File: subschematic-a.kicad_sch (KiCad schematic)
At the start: 0 parts

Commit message: chore(template): prepare Boardwright CI test
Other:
- title: Sheet Title A -> SUB SCHEMATIC A
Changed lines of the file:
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@@
 	(paper "A4")
 	(title_block
-		(title "Sheet Title A")
+		(title "SUB SCHEMATIC A")
 		(date "2025-01-12")
 		(rev "${REVISION}")
@@
 	(text_box "[${#}] ${TITLE}"
 		(exclude_from_sim no)
-		(at 99.06 15 0)
-		(size 107.9128 15)
+		(at 20.32 10.16 0)
+		(size 266.7 20.32)
 		(margins 4.4999 4.4999 4.4999 4.4999)
 		(stroke

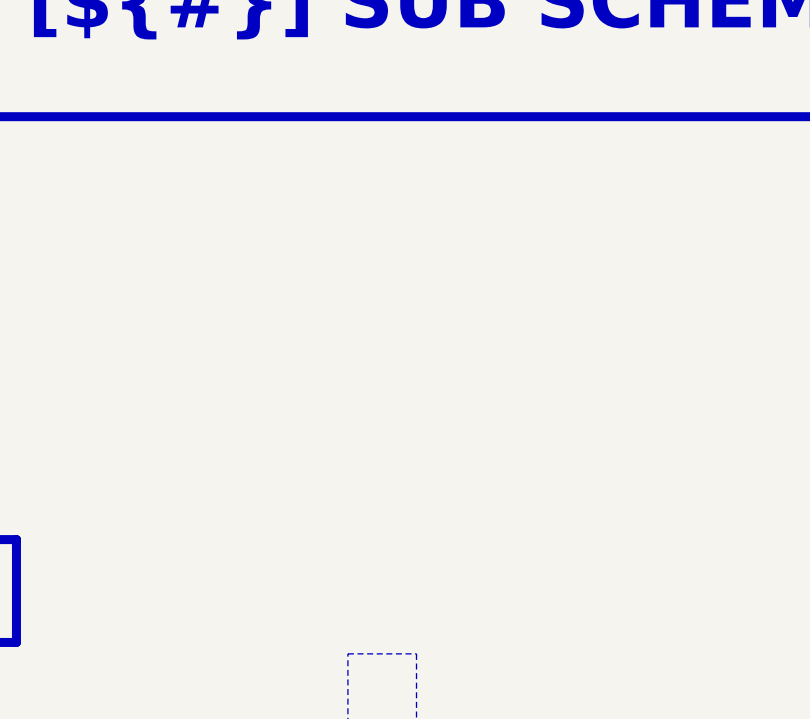
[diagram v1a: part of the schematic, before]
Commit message: feat(hardware): add Boardwright CI fixture circuit
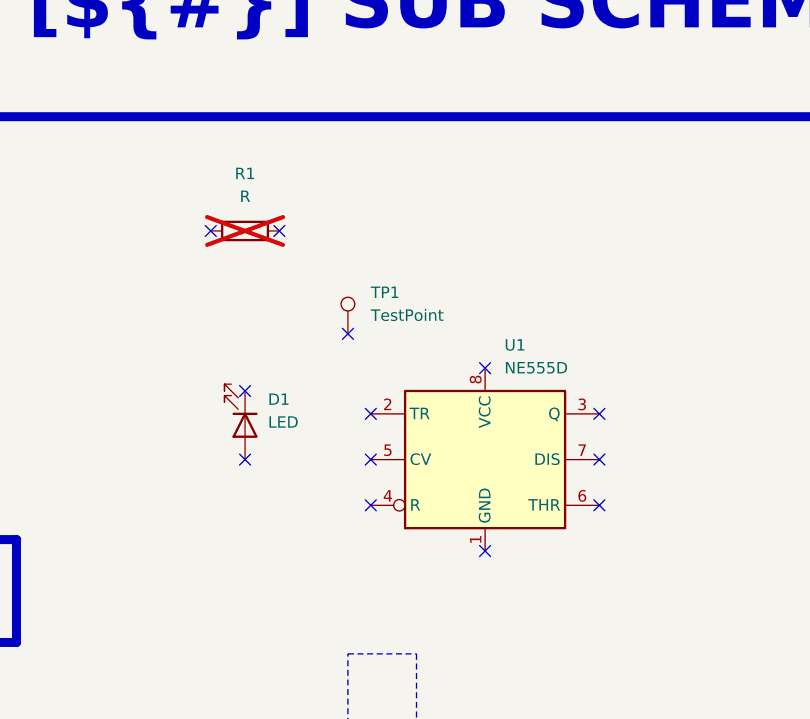
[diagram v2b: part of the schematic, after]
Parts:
- added D1: LED, LED_THT:LED_D5.0mm_FlatTop, symbol Device:LED
- added R1: R, Resistor_THT:R_Axial_DIN0617_L17.0mm_D6.0mm_P30.48mm_Horizontal, symbol Device:R
- added TP1: TestPoint, RD-Testpoints:TestPoint_Pad_D1.5mm, symbol Connector:TestPoint
- added U1: NE555D, Package_SO:SOIC-8_3.9x4.9mm_P1.27mm, symbol Timer:NE555D
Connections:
- no-connect marks 0 -> 13
